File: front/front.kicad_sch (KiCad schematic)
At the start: 0 parts

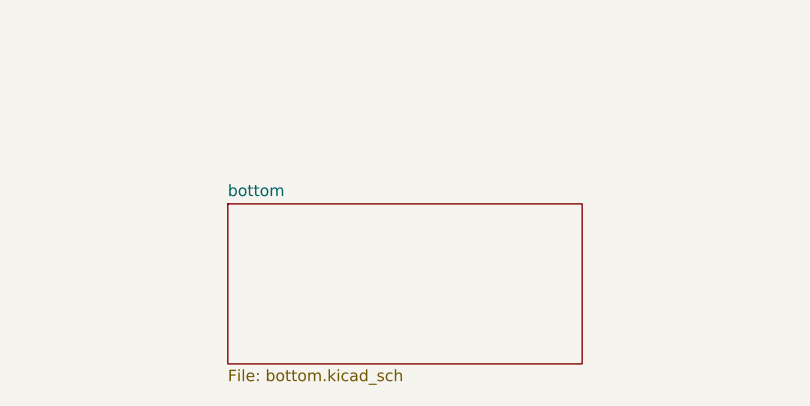
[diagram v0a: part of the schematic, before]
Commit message: undo panelizing
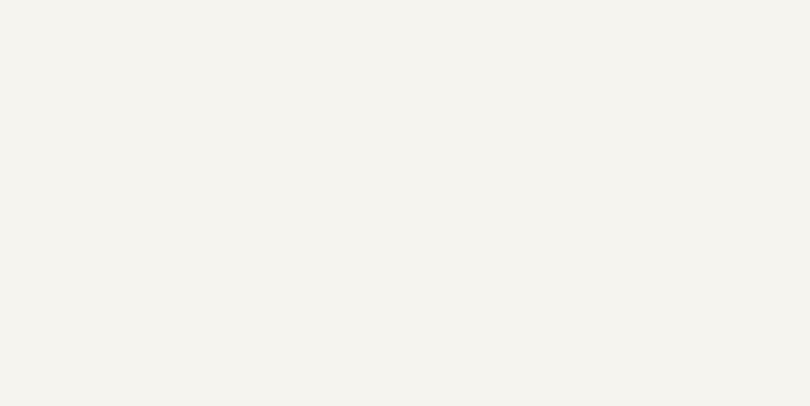
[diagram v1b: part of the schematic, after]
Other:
- removed sheet bottom
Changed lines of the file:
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@@
-		)
-	)
-	(sheet
-		(at 97.79 116.84)
-		(size 39.37 17.78)
-		(exclude_from_sim no)
-		(in_bom yes)
-		(on_board yes)
-		(dnp no)
-		(fields_autoplaced yes)
-		(stroke
-			(width 0.1524)
-			(type solid)
-		)
-		(fill
-			(color 0 0 0 0.0000)
-		)
-		(property "Sheetname" "bottom"
-			(at 97.79 116.1284 0)
-			(effects
-				(font
-					(size 1.27 1.27)
-				)
-				(justify left bottom)
-			)
-		)
-		(property "Sheetfile" "bottom.kicad_sch"
-			(at 97.79 135.2046 0)
-			(effects
-				(font
-					(size 1.27 1.27)
-				)
-				(justify left top)
-			)
-		)
-		(instances
-			(project "front"
-				(path "/508f986b-6f1b-4c39-bd57-bae69573a4e7"
-					(page "4")
-				)
-			)
 		)
 	)

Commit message: begin layout
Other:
- note added: "1.8 @ 90mA 3.3 @ 60mA"
- note added: "1.8v buck 300mA"
- note added: "3.3 LDO"
- note added: "3.3v @ 150"
- note added: "3.3v @ ~50"
- note added: "3.3v buck 600mA"
- note added: "battery (3.5-5.1)"
- note added: "components count: 14, cost: $6 efficiency ~90%"
- note added: "https://webench.ti.com/appinfo/webench/scripts/SDP.cgi?ID=4D8F5999841C80F8"
- note added: "https://webench.ti.com/appinfo/webench/scripts/SDP.cgi?ID=7CF6C6E15C89EFE1"
- note added: "i2c extender IMU"
- note added: "long wires"
- note added: "power supply components count: ~21, cost: $3 efficiency: ~70%"
- note added: "vl53l8cx"
